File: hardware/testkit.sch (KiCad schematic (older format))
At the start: 3 parts, among them J5 Left, J6 Right, J7 Bottom

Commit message: Finish up first plausible version
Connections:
- net GND: now reaches J5.1 (Pin_1)
- net GND: now also J5.10 (Pin_10), J5.13 (Pin_13), J5.14 (Pin_14), J5.2 (Pin_2), J5.27 (Pin_27), J5.28 (Pin_28), J5.39 (Pin_39), J5.40 (Pin_40), J5.5 (Pin_5), J5.6 (Pin_6), J5.9 (Pin_9), J6.1 (Pin_1), J6.13 (Pin_13), J6.14 (Pin_14), J6.19 (Pin_19), J6.2 (Pin_2), J6.20 (Pin_20), J6.29 (Pin_29), J6.30 (Pin_30), J6.39 (Pin_39), J6.40 (Pin_40), J7.1 (Pin_1), J7.10 (Pin_10), J7.12 (Pin_12), J7.14 (Pin_14), J7.16 (Pin_16), J7.18 (Pin_18), J7.2 (Pin_2), J7.20 (Pin_20), J7.21 (Pin_21), J7.22 (Pin_22), J7.24 (Pin_24), J7.26 (Pin_26), J7.28 (Pin_28), J7.3 (Pin_3), J7.30 (Pin_30), J7.32 (Pin_32), J7.34 (Pin_34), J7.36 (Pin_36), J7.38 (Pin_38), J7.39 (Pin_39), J7.4 (Pin_4), J7.40 (Pin_40), J7.5 (Pin_5), J7.6 (Pin_6), J7.8 (Pin_8)
- net +3V3: now reaches J5.11 (Pin_11)
- net +3V3: now also J5.12 (Pin_12)
- net A1-PRE: now reaches J5.15 (Pin_15)
- net A2-PRE: now reaches J5.16 (Pin_16)
- net A3-PRE: now reaches J5.17 (Pin_17)
- net A4-PRE: now reaches J5.18 (Pin_18)
- net A5-PRE: now reaches J5.19 (Pin_19)
- net A6-PRE: now reaches J5.20 (Pin_20)
- net A7-PRE: now reaches J5.21 (Pin_21)
- net A8-PRE: now reaches J5.22 (Pin_22)
- net A9-PRE: now reaches J5.23 (Pin_23)
- net A10-PRE: now reaches J5.24 (Pin_24)
- net A11-PRE: now reaches J5.25 (Pin_25)
- net A12-PRE: now reaches J5.26 (Pin_26)
- net A13: now reaches J5.29 (Pin_29)
- net +12VDOWNSTREAM: now reaches J5.3 (Pin_3)
- net +12VDOWNSTREAM: now also J5.4 (Pin_4)
- net A14: now reaches J5.30 (Pin_30)
- net A15: now reaches J5.31 (Pin_31)
- net A16: now reaches J5.32 (Pin_32)
- net A18: now reaches J5.33 (Pin_33)
- net A17: now reaches J5.34 (Pin_34)
- net A20: now reaches J5.35 (Pin_35)
- net A19: now reaches J5.36 (Pin_36)
- net -12VDOWNSTREAM: now reaches J5.7 (Pin_7)
- net -12VDOWNSTREAM: now also J5.8 (Pin_8)
- net SERIAL4.0: now reaches J7.11 (Pin_11)
- net SERIAL4.1: now reaches J7.13 (Pin_13)
- net SERIAL4.2: now reaches J7.15 (Pin_15)
- net SERIAL4.3: now reaches J7.17 (Pin_17)
- net DB0: now reaches J7.19 (Pin_19)
- net SERIAL1.0: now reaches J7.23 (Pin_23)
- net SERIAL1.1: now reaches J7.25 (Pin_25)
- net SERIAL1.2: now reaches J7.27 (Pin_27)
- net SERIAL1.3: now reaches J7.29 (Pin_29)
- net DR4: now reaches J7.31 (Pin_31)
- net DR3: now reaches J7.33 (Pin_33)
- net DR2: now reaches J7.35 (Pin_35)
- net DR1: now reaches J7.37 (Pin_37)
- net DB1: now reaches J7.7 (Pin_7)
- net DB2: now reaches J7.9 (Pin_9)
- net AUDIO_IN_1A: now reaches J6.10 (Pin_10)
- net AUDIO_IN_1C: now reaches J6.11 (Pin_11)
- net AUDIO_IN_1D: now reaches J6.12 (Pin_12)
- net OSC_D: now reaches J6.15 (Pin_15)
- net OSC_C: now reaches J6.16 (Pin_16)
- net OSC_B: now reaches J6.17 (Pin_17)
- net OSC_A: now reaches J6.18 (Pin_18)
- net DAC_2B: now reaches J6.21 (Pin_21)
- net DAC_2A: now reaches J6.22 (Pin_22)
- net DAC_2C: now reaches J6.23 (Pin_23)
- net DAC_2D: now reaches J6.24 (Pin_24)
- net DAC_1B: now reaches J6.25 (Pin_25)
- net DAC_1A: now reaches J6.26 (Pin_26)
- net DAC_1C: now reaches J6.27 (Pin_27)
- net DAC_1D: now reaches J6.28 (Pin_28)
- net AUDIO_OUT_L: now reaches J6.3 (Pin_3)
- net DAC_4B: now reaches J6.31 (Pin_31)
- net DAC_4A: now reaches J6.32 (Pin_32)
- net DAC_4C: now reaches J6.33 (Pin_33)
- net DAC_4D: now reaches J6.34 (Pin_34)
- net DAC_3B: now reaches J6.35 (Pin_35)
- net DAC_3A: now reaches J6.36 (Pin_36)
- net DAC_3C: now reaches J6.37 (Pin_37)
- net DAC_3D: now reaches J6.38 (Pin_38)
- net AUDIO_OUT_R: now reaches J6.4 (Pin_4)
- net AUDIO_IN_2B: now reaches J6.5 (Pin_5)
- net AUDIO_IN_2A: now reaches J6.6 (Pin_6)
- net AUDIO_IN_2C: now reaches J6.7 (Pin_7)
- net AUDIO_IN_2D: now reaches J6.8 (Pin_8)
- net AUDIO_IN_1B: now reaches J6.9 (Pin_9)
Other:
- moved on the sheet: J6, J7

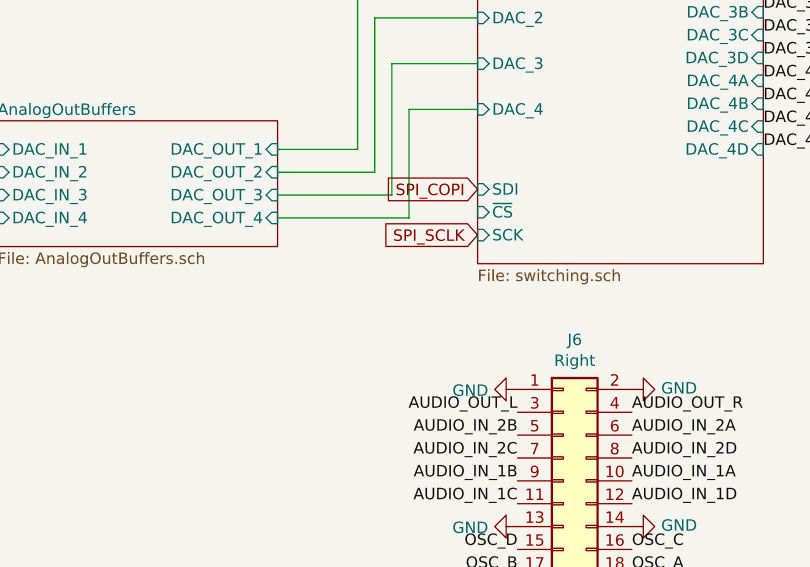
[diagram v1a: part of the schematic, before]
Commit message: Make note that I forgot to wire up CS for the switches
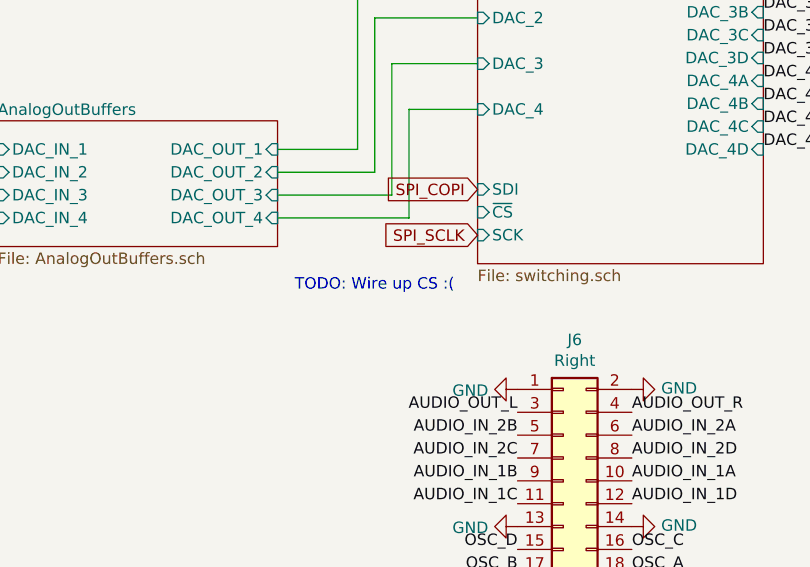
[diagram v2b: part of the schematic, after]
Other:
- note added: "TODO: Wire up CS :("
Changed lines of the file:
@@
 	0    1    1    0
 $EndComp
+Text Notes 6050 4075 0    50   ~ 0
+TODO: Wire up CS :(
 $EndSCHEMATC
